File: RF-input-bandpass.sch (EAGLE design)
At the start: 9 parts, among them J2 DC 0 AC 1E-6

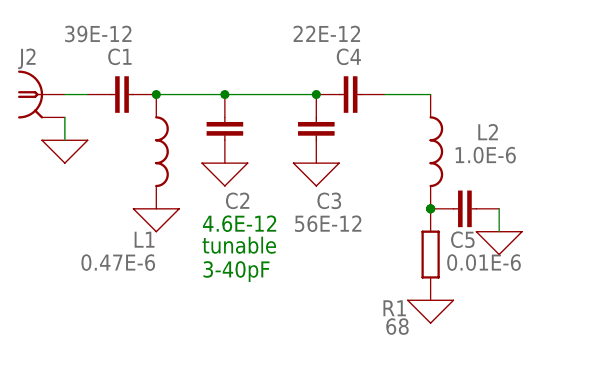
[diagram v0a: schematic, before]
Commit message: Generate RF input bandpass board
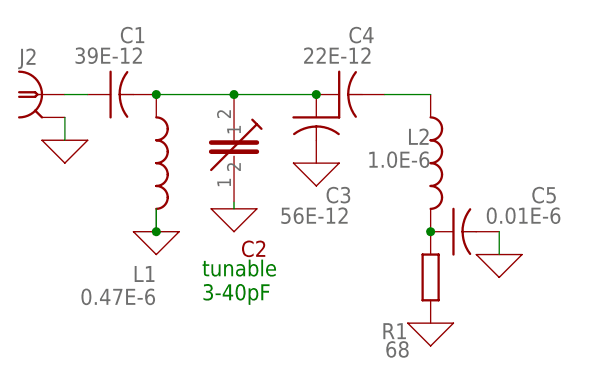
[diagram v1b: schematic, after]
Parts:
- C1, C3, C4, C5: device ngspice-simulation:C -> rcl:C-US025-024X044; SPICEPREFIX C -> (none)
- C2: device ngspice-simulation:C -> sprague-goodman:GYC20000
- L1, L2: device ngspice-simulation:L -> rcl:L-US0204/5; SPICEPREFIX L -> (none)
- R1: SPICEPREFIX R -> (none)
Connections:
- net 0: now also C2.1; no longer C2.2
- net N$2: now also C2.2; no longer C2.1
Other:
- moved on the sheet: C5, R1

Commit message: Add missing R1 to brd, invert layout png colors
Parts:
- R1: device ngspice-simulation:R -> adafruit:R-US_0204/2V; SPICEPREFIX (none) -> R
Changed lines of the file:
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@@
 <part name="X_5" library="ngspice-simulation" library_urn="urn:adsk.eagle:library:527439" deviceset="GND" device=""/>
 <part name="X_6" library="ngspice-simulation" library_urn="urn:adsk.eagle:library:527439" deviceset="GND" device=""/>
-<part name="R1" library="ngspice-simulation" library_urn="urn:adsk.eagle:library:527439" deviceset="R" device="" value="68">
-<spice>
-<pinmapping spiceprefix="R">
-<pinmap gate="G$1" pin="1" pinorder="1"/>
-<pinmap gate="G$1" pin="2" pinorder="2"/>
-</pinmapping>
-</spice>
-</part>
 <part name="C2" library="sprague-goodman" deviceset="GYC20000" device="" value="4.6E-12">
 <spice>
@@
 <part name="C4" library="rcl" library_urn="urn:adsk.eagle:library:334" deviceset="C-US" device="025-024X044" package3d_urn="urn:adsk.eagle:package:23630/1" value="22E-12"/>
 <part name="C5" library="rcl" library_urn="urn:adsk.eagle:library:334" deviceset="C-US" device="025-024X044" package3d_urn="urn:adsk.eagle:package:23630/1" value="0.01E-6"/>
+<part name="R1" library="adafruit" library_urn="urn:adsk.eagle:library:420" deviceset="R-US_" device="0204/2V" package3d_urn="urn:adsk.eagle:package:6240630/1" value="68">
+<spice>
+<pinmapping isusermap="yes" isdevicewide="yes">
+<pinmap gate="G$1" pin="1" pinorder="2"/>
+<pinmap gate="G$1" pin="2" pinorder="1"/>
+</pinmapping>
+</spice>
+<attribute name="SPICEPREFIX" value="R"/>
+</part>
 </parts>
 <sheets>
@@
 <instance part="X_5" gate="G$1" x="30.48" y="71.12" smashed="yes"/>
 <instance part="X_6" gate="G$1" x="22.86" y="63.5" smashed="yes"/>
-<instance part="R1" gate="G$1" x="22.86" y="68.58" smashed="yes" rot="R90">
-<attribute name="NAME" x="20.32" y="63.5" size="1.778" layer="95" rot="R180"/>
-<attribute name="VALUE" x="17.78" y="59.69" size="1.778" layer="96"/>
-</instance>
 <instance part="C2" gate="G$1" x="1.016" y="83.058" smashed="yes" rot="MR90">
 <attribute name="NAME" x="1.778" y="72.644" size="1.778" layer="94" rot="MR180"/>
@@
 <attribute name="NAME" x="34.036" y="76.835" size="1.778" layer="95"/>
 <attribute name="VALUE" x="28.956" y="74.549" size="1.778" layer="96"/>
+</instance>
+<instance part="R1" gate="G$1" x="22.86" y="68.58" smashed="yes" rot="R90">
+<attribute name="NAME" x="21.59" y="69.6214" size="1.778" layer="95" rot="R180"/>
+<attribute name="VALUE" x="21.59" y="66.802" size="1.778" layer="96" rot="R180"/>
 </instance>
 </instances>
@@
 <net name="N$4" class="0">
 <segment>
-<pinref part="R1" gate="G$1" pin="2"/>
 <pinref part="L2" gate="G$1" pin="2"/>
 <pinref part="C5" gate="G$1" pin="1"/>
+<pinref part="R1" gate="G$1" pin="2"/>
 <junction x="22.86" y="73.66"/>
 </segment>
 </net>
 <net name="0" class="0">
-<segment>
-<pinref part="R1" gate="G$1" pin="1"/>
-<pinref part="X_6" gate="G$1" pin="0"/>
-</segment>
 <segment>
 <pinref part="X_5" gate="G$1" pin="0"/>
@@
 <pinref part="C3" gate="G$1" pin="2"/>
 </segment>
+<segment>
+<pinref part="X_6" gate="G$1" pin="0"/>
+<pinref part="R1" gate="G$1" pin="1"/>
+</segment>
 </net>
